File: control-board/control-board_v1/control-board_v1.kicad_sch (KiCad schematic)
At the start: 57 parts, among them J1 Barrel_Jack, J2 PH2-12-UA, J3 PH2-12-UA, J4 PH2-12-UA, J5 PH2-12-UA, J6 Conn_01x08_Socket, J7 Conn_01x06_Socket, J8 Conn_01x10_Socket, J9 Conn_01x08_Socket, Q1 Q_Dual_PMOS_S1G1D2S2G2D1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

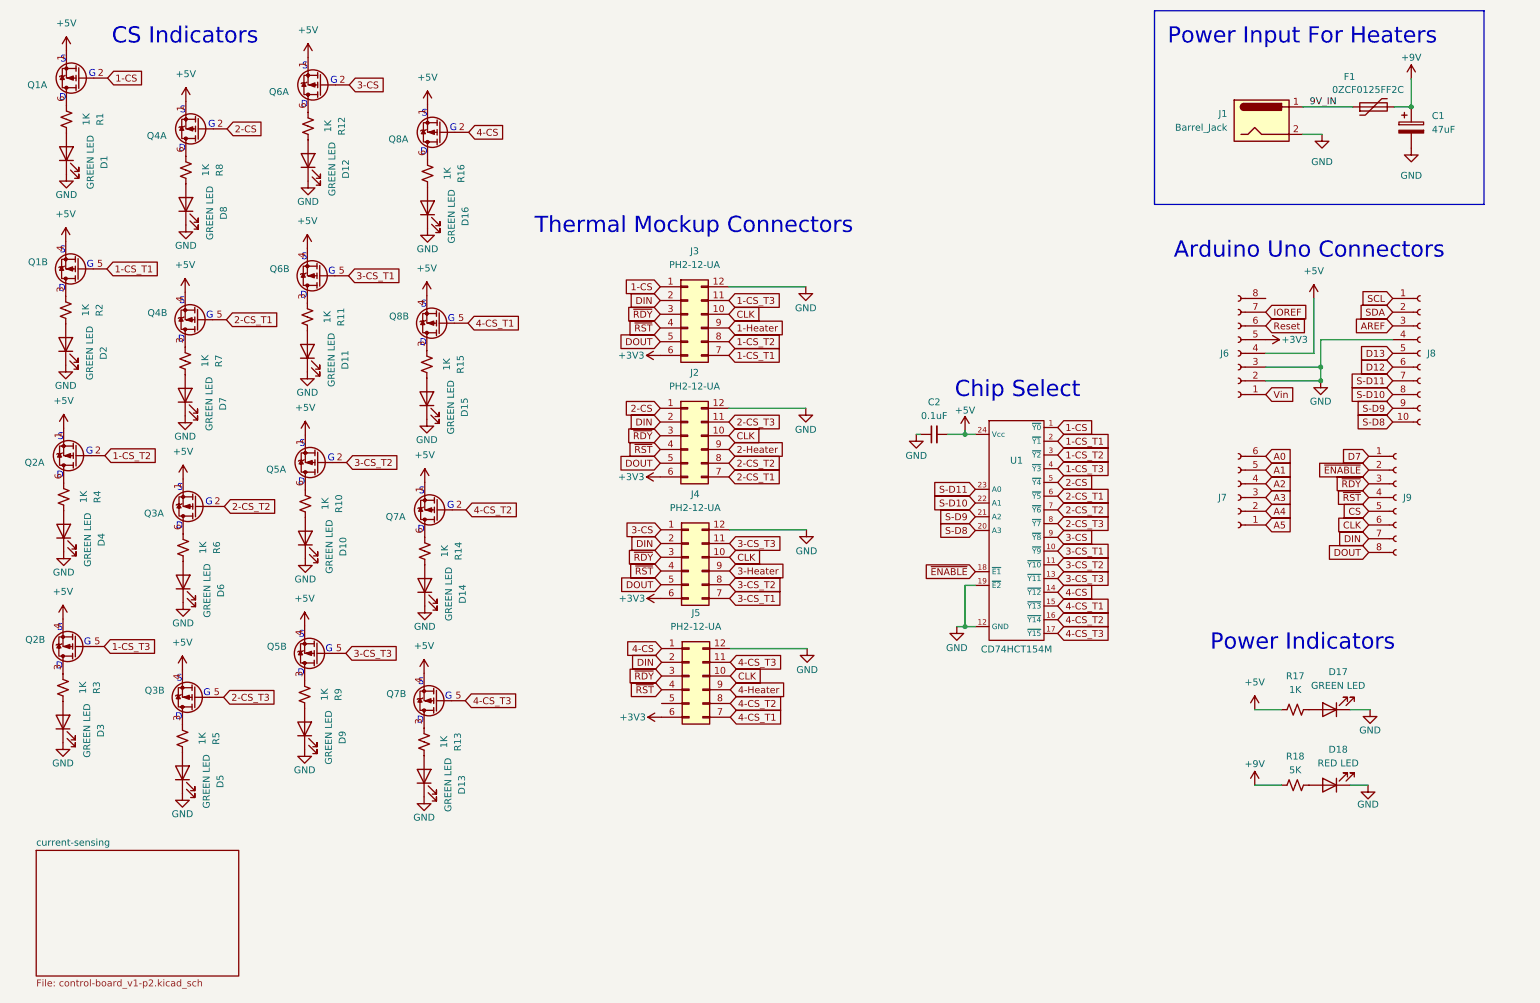
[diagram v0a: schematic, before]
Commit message: added opamp to reduce adc signals
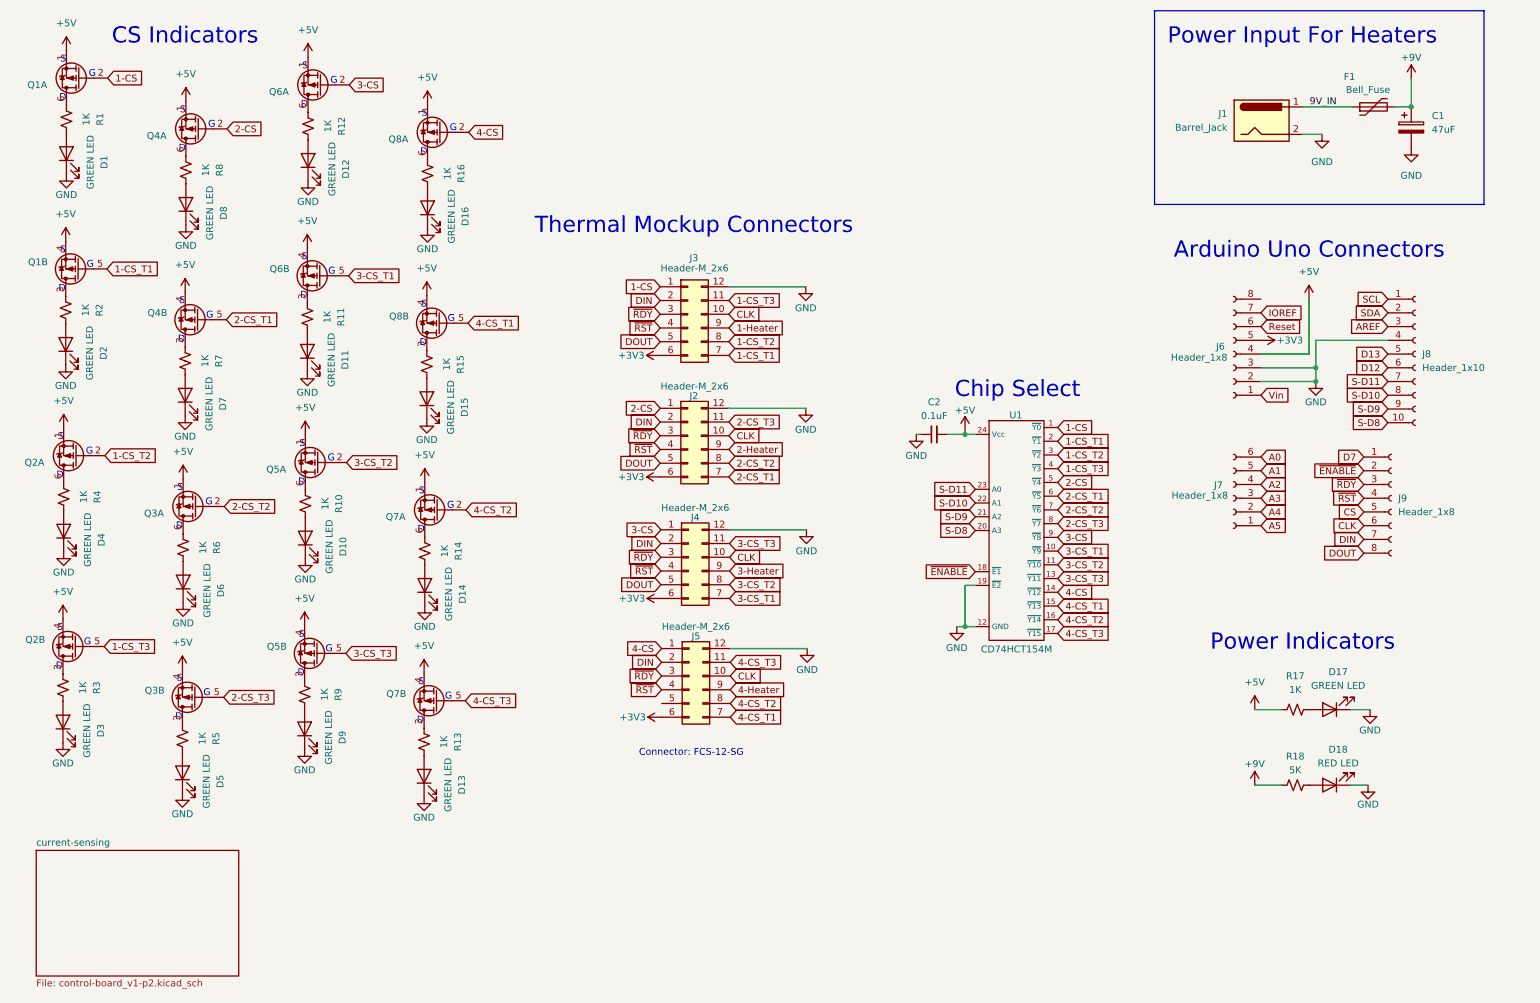
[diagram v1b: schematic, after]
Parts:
- F1: value 0ZCF0125FF2C -> Bell_Fuse; Mfg Bel Fuse -> (none); PartNum 0ZCF0125FF2C -> 0ZCF0250FF2C
- J1: Mfg CUI -> (none)
- J2, J3, J4, J5: value PH2-12-UA -> Header-M_2x6; PartNum (none) -> 5-146130-5
- J6, J9: value Conn_01x08_Socket -> Header_1x8; PartNum (none) -> ESQ-108-14-T-S
- J7: value Conn_01x06_Socket -> Header_1x8; PartNum (none) -> ESQ-106-14-T-S
- J8: value Conn_01x10_Socket -> Header_1x10; PartNum (none) -> ESQ-110-14-T-S
- Q1, Q2, Q3, Q4, Q5, Q6, Q7, Q8: value Q_Dual_PMOS_S1G1D2S2G2D1 -> PMOS; PartNum (none) -> SI1967DH-T1-BE3
- U1: PartNum (none) -> CD74HCT154M
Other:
- note added: "Connector: FCS-12-SG"
- moved on the sheet: J6, J7, J8, J9

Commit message: added gain op-amp
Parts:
- D1, D2, D3, D4: value GREEN LED -> BLUE LED
- D10, D11, D12, D9: value GREEN LED -> RED LED
- D13, D14, D15, D16: value GREEN LED -> YELLOW LED
- D18: value RED LED -> ORANGE LED
- D5, D6, D7, D8: value GREEN LED -> WHITE LED
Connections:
- net D12 renamed H1-D12
- net D13 renamed H2-D13
- net SCL renamed H4-D19
- net SDA renamed H3-D18
- no-connect marks 0 -> 1

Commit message: fixed footprint matching
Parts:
- D1, D10, D11, D12, D13, D14, D15, D16, D17, D18, D2, D3, D4, D5, D6, D7, D8, D9: footprint LED_SMD:LED_0805_2012Metric -> LED_SMD:LED_0603_1608Metric
- Q1, Q2, Q3, Q4, Q5, Q6, Q7, Q8: footprint (none) -> Package_TO_SOT_SMD:SOT-363_SC-70-6
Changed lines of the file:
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@@
       (effects (font (size 1.27 1.27)) (justify left))
     )
-    (property "Footprint" "" (at 88.773 105.918 0)
+    (property "Footprint" "Package_TO_SOT_SMD:SOT-363_SC-70-6" (at 88.773 105.918 0)
       (effects (font (size 1.27 1.27)) hide)
     )
@@
       (effects (font (size 1.27 1.27)) (justify right))
     )
-    (property "Footprint" "LED_SMD:LED_0805_2012Metric" (at 65.786 76.581 0)
+    (property "Footprint" "LED_SMD:LED_0603_1608Metric" (at 65.786 76.581 0)
       (effects (font (size 1.27 1.27)) hide)
     )
@@
       (effects (font (size 1.27 1.27)) (justify right))
     )
-    (property "Footprint" "LED_SMD:LED_0805_2012Metric" (at 65.278 146.431 0)
+    (property "Footprint" "LED_SMD:LED_0603_1608Metric" (at 65.278 146.431 0)
       (effects (font (size 1.27 1.27)) hide)
     )
@@
       (effects (font (size 1.27 1.27)) (justify left))
     )
-    (property "Footprint" "" (at 89.281 36.068 0)
+    (property "Footprint" "Package_TO_SOT_SMD:SOT-363_SC-70-6" (at 89.281 36.068 0)
       (effects (font (size 1.27 1.27)) hide)
     )
@@
       (effects (font (size 1.27 1.27)) (justify left))
     )
-    (property "Footprint" "" (at 43.942 140.589 0)
+    (property "Footprint" "Package_TO_SOT_SMD:SOT-363_SC-70-6" (at 43.942 140.589 0)
       (effects (font (size 1.27 1.27)) hide)
     )
@@
       (effects (font (size 1.27 1.27)) (justify right))
     )
-    (property "Footprint" "LED_SMD:LED_0805_2012Metric" (at 87.884 85.344 0)
+    (property "Footprint" "LED_SMD:LED_0603_1608Metric" (at 87.884 85.344 0)
       (effects (font (size 1.27 1.27)) hide)
     )
@@
       (effects (font (size 1.27 1.27)) (justify right))
     )
-    (property "Footprint" "LED_SMD:LED_0805_2012Metric" (at 65.405 111.125 0)
+    (property "Footprint" "LED_SMD:LED_0603_1608Metric" (at 65.405 111.125 0)
       (effects (font (size 1.27 1.27)) hide)
     )
@@
       (effects (font (size 1.27 1.27)) (justify right))
     )
-    (property "Footprint" "LED_SMD:LED_0805_2012Metric" (at 65.913 41.275 0)
+    (property "Footprint" "LED_SMD:LED_0603_1608Metric" (at 65.913 41.275 0)
       (effects (font (size 1.27 1.27)) hide)
     )
@@
       (effects (font (size 1.27 1.27)))
     )
-    (property "Footprint" "LED_SMD:LED_0805_2012Metric" (at 254.889 156.845 0)
+    (property "Footprint" "LED_SMD:LED_0603_1608Metric" (at 254.889 156.845 0)
       (effects (font (size 1.27 1.27)) hide)
     )
@@
       (effects (font (size 1.27 1.27)) (justify right))
     )
-    (property "Footprint" "LED_SMD:LED_0805_2012Metric" (at 20.701 109.855 0)
+    (property "Footprint" "LED_SMD:LED_0603_1608Metric" (at 20.701 109.855 0)
       (effects (font (size 1.27 1.27)) hide)
     )
@@
       (effects (font (size 1.27 1.27)) (justify right))
     )
-    (property "Footprint" "LED_SMD:LED_0805_2012Metric" (at 43.18 84.709 0)
+    (property "Footprint" "LED_SMD:LED_0603_1608Metric" (at 43.18 84.709 0)
       (effects (font (size 1.27 1.27)) hide)
     )
@@
       (effects (font (size 1.27 1.27)) (justify left))
     )
-    (property "Footprint" "" (at 67.056 62.611 0)
+    (property "Footprint" "Package_TO_SOT_SMD:SOT-363_SC-70-6" (at 67.056 62.611 0)
       (effects (font (size 1.27 1.27)) hide)
     )
@@
       (effects (font (size 1.27 1.27)) (justify right))
     )
-    (property "Footprint" "LED_SMD:LED_0805_2012Metric" (at 20.574 145.161 0)
+    (property "Footprint" "LED_SMD:LED_0603_1608Metric" (at 20.574 145.161 0)
       (effects (font (size 1.27 1.27)) hide)
     )
@@
       (effects (font (size 1.27 1.27)) (justify right))
     )
-    (property "Footprint" "LED_SMD:LED_0805_2012Metric" (at 42.672 154.559 0)
+    (property "Footprint" "LED_SMD:LED_0603_1608Metric" (at 42.672 154.559 0)
       (effects (font (size 1.27 1.27)) hide)
     )
@@
       (effects (font (size 1.27 1.27)) (justify right))
     )
-    (property "Footprint" "LED_SMD:LED_0805_2012Metric" (at 88.011 50.038 0)
+    (property "Footprint" "LED_SMD:LED_0603_1608Metric" (at 88.011 50.038 0)
       (effects (font (size 1.27 1.27)) hide)
     )
@@
       (effects (font (size 1.27 1.27)) (justify right))
     )
-    (property "Footprint" "LED_SMD:LED_0805_2012Metric" (at 42.799 119.253 0)
+    (property "Footprint" "LED_SMD:LED_0603_1608Metric" (at 42.799 119.253 0)
       (effects (font (size 1.27 1.27)) hide)
     )
@@
       (effects (font (size 1.27 1.27)) (justify right))
     )
-    (property "Footprint" "LED_SMD:LED_0805_2012Metric" (at 21.082 75.311 0)
+    (property "Footprint" "LED_SMD:LED_0603_1608Metric" (at 21.082 75.311 0)
       (effects (font (size 1.27 1.27)) hide)
     )
@@
       (effects (font (size 1.27 1.27)) (justify left))
     )
-    (property "Footprint" "" (at 66.548 132.461 0)
+    (property "Footprint" "Package_TO_SOT_SMD:SOT-363_SC-70-6" (at 66.548 132.461 0)
       (effects (font (size 1.27 1.27)) hide)
     )
@@
       (effects (font (size 1.27 1.27)) (justify left))
     )
-    (property "Footprint" "" (at 21.971 95.885 0)
+    (property "Footprint" "Package_TO_SOT_SMD:SOT-363_SC-70-6" (at 21.971 95.885 0)
       (effects (font (size 1.27 1.27)) hide)
     )
@@
       (effects (font (size 1.27 1.27)) (justify left))
     )
-    (property "Footprint" "" (at 89.154 71.374 0)
+    (property "Footprint" "Package_TO_SOT_SMD:SOT-363_SC-70-6" (at 89.154 71.374 0)
       (effects (font (size 1.27 1.27)) hide)
     )
@@
       (effects (font (size 1.27 1.27)) (justify left))
     )
-    (property "Footprint" "" (at 22.479 26.035 0)
+    (property "Footprint" "Package_TO_SOT_SMD:SOT-363_SC-70-6" (at 22.479 26.035 0)
       (effects (font (size 1.27 1.27)) hide)
     )
@@
       (effects (font (size 1.27 1.27)) (justify left))
     )
-    (property "Footprint" "" (at 44.069 105.283 0)
+    (property "Footprint" "Package_TO_SOT_SMD:SOT-363_SC-70-6" (at 44.069 105.283 0)
       (effects (font (size 1.27 1.27)) hide)
     )
@@
       (effects (font (size 1.27 1.27)) (justify left))
     )
-    (property "Footprint" "" (at 88.646 141.224 0)
+    (property "Footprint" "Package_TO_SOT_SMD:SOT-363_SC-70-6" (at 88.646 141.224 0)
       (effects (font (size 1.27 1.27)) hide)
     )
@@
       (effects (font (size 1.27 1.27)) (justify right))
     )
-    (property "Footprint" "LED_SMD:LED_0805_2012Metric" (at 87.376 155.194 0)
+    (property "Footprint" "LED_SMD:LED_0603_1608Metric" (at 87.376 155.194 0)
       (effects (font (size 1.27 1.27)) hide)
     )
@@
       (effects (font (size 1.27 1.27)) (justify left))
     )
-    (property "Footprint" "" (at 21.844 131.191 0)
+    (property "Footprint" "Package_TO_SOT_SMD:SOT-363_SC-70-6" (at 21.844 131.191 0)
       (effects (font (size 1.27 1.27)) hide)
     )
@@
       (effects (font (size 1.27 1.27)) (justify left))
     )
-    (property "Footprint" "" (at 22.352 61.341 0)
+    (property "Footprint" "Package_TO_SOT_SMD:SOT-363_SC-70-6" (at 22.352 61.341 0)
       (effects (font (size 1.27 1.27)) hide)
     )
@@
       (effects (font (size 1.27 1.27)) (justify left))
     )
-    (property "Footprint" "" (at 44.577 35.433 0)
+    (property "Footprint" "Package_TO_SOT_SMD:SOT-363_SC-70-6" (at 44.577 35.433 0)
       (effects (font (size 1.27 1.27)) hide)
     )
@@
       (effects (font (size 1.27 1.27)) (justify left))
     )
-    (property "Footprint" "" (at 66.675 97.155 0)
+    (property "Footprint" "Package_TO_SOT_SMD:SOT-363_SC-70-6" (at 66.675 97.155 0)
       (effects (font (size 1.27 1.27)) hide)
     )
@@
       (effects (font (size 1.27 1.27)) (justify left))
     )
-    (property "Footprint" "" (at 67.183 27.305 0)
+    (property "Footprint" "Package_TO_SOT_SMD:SOT-363_SC-70-6" (at 67.183 27.305 0)
       (effects (font (size 1.27 1.27)) hide)
     )
@@
       (effects (font (size 1.27 1.27)) (justify right))
     )
-    (property "Footprint" "LED_SMD:LED_0805_2012Metric" (at 87.503 119.888 0)
+    (property "Footprint" "LED_SMD:LED_0603_1608Metric" (at 87.503 119.888 0)
       (effects (font (size 1.27 1.27)) hide)
     )
@@
       (effects (font (size 1.27 1.27)) (justify left))
     )
-    (property "Footprint" "" (at 44.45 70.739 0)
+    (property "Footprint" "Package_TO_SOT_SMD:SOT-363_SC-70-6" (at 44.45 70.739 0)
       (effects (font (size 1.27 1.27)) hide)
     )
@@
       (effects (font (size 1.27 1.27)))
     )
-    (property "Footprint" "LED_SMD:LED_0805_2012Metric" (at 254.889 142.875 0)
+    (property "Footprint" "LED_SMD:LED_0603_1608Metric" (at 254.889 142.875 0)
       (effects (font (size 1.27 1.27)) hide)
     )
@@
       (effects (font (size 1.27 1.27)) (justify right))
     )
-    (property "Footprint" "LED_SMD:LED_0805_2012Metric" (at 43.307 49.403 0)
+    (property "Footprint" "LED_SMD:LED_0603_1608Metric" (at 43.307 49.403 0)
       (effects (font (size 1.27 1.27)) hide)
     )
@@
       (effects (font (size 1.27 1.27)) (justify right))
     )
-    (property "Footprint" "LED_SMD:LED_0805_2012Metric" (at 21.209 40.005 0)
+    (property "Footprint" "LED_SMD:LED_0603_1608Metric" (at 21.209 40.005 0)
       (effects (font (size 1.27 1.27)) hide)
     )
